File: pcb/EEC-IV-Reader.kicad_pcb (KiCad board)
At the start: 2 copper layers, 53 x 68.7 mm, 39 parts, among them J1 ARDUINO_1, J2 ARDUINO_2, J3 RS_485_DEBUG, J4 ARDUINO_3, J5 ARDUINO_4, J6 DISPLAY, J7 OBD, J8 I2C_DEBUG, J9 Vin_disconnect, SW1 BTN_UP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

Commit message: Update LED Labels and Diode direction
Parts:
- moved D2 7.60 mm to (87.6, 61.3), turned to 180 degrees
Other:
- board text added: "IN"
- board text added: "OUT"
- board text added: "v0.4"
- board text removed: "DI"
- board text removed: "RO"
- board text removed: "v0.3"
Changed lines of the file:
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@@
   )
   (footprint "Diode_THT:D_A-405_P7.62mm_Horizontal" (layer "F.Cu")
-    (at 80 61.3)
+    (at 87.6 61.3 180)
     (descr "Diode, A-405 series, Axial, Horizontal, pin pitch=7.62mm, , length*diameter=5.2*2.7mm^2, , http://www.diodes.com/_files/packages/A-405.pdf")
     (tags "Diode A-405 series Axial Horizontal pin pitch 7.62mm  length 5.2mm diameter 2.7mm")
@@
     (property "Sheetname" "")
     (attr through_hole)
-    (fp_text reference "D2" (at 3.81 -2.47) (layer "F.SilkS")
+    (fp_text reference "D2" (at 3.85 2.3) (layer "F.SilkS")
       (effects (font (size 1 1) (thickness 0.15)))
     )
@@
     (fp_line (start 1.21 -1.35) (end 1.21 1.35) (layer "F.Fab") (width 0.1))
     (fp_line (start 1.89 -1.35) (end 1.89 1.35) (layer "F.Fab") (width 0.1))
-    (pad "1" thru_hole rect (at 0 0) (size 1.8 1.8) (drill 0.9) (layers *.Cu *.Mask)
+    (pad "1" thru_hole rect (at 0 0 180) (size 1.8 1.8) (drill 0.9) (layers *.Cu *.Mask)
       (net 36 "/8V") (pinfunction "K") (pintype "passive"))
-    (pad "2" thru_hole oval (at 7.62 0) (size 1.8 1.8) (drill 0.9) (layers *.Cu *.Mask)
+    (pad "2" thru_hole oval (at 7.62 0 180) (size 1.8 1.8) (drill 0.9) (layers *.Cu *.Mask)
       (net 5 "Net-(D2-Pad2)") (pinfunction "A") (pintype "passive"))
     (model "${KICAD6_3DMODEL_DIR}/Diode_THT.3dshapes/D_A-405_P7.62mm_Horizontal.wrl"
@@
     (effects (font (size 1 1) (thickness 0.1)))
   )
-  (gr_text "DI" (at 56 78.9) (layer "F.SilkS")
-    (effects (font (size 1 1) (thickness 0.1)))
-  )
-  (gr_text "v0.3" (at 43.771725 88.904421) (layer "F.SilkS")
+  (gr_text "OUT" (at 56.3 79.05) (layer "F.SilkS")
+    (effects (font (size 1 1) (thickness 0.1)))
+  )
+  (gr_text "v0.4" (at 43.771725 88.904421) (layer "F.SilkS")
     (effects (font (size 1 1) (thickness 0.15)) (justify left))
   )
@@
     (effects (font (size 1 1) (thickness 0.1)))
   )
-  (gr_text "RO" (at 56.2 73.5) (layer "F.SilkS")
-    (effects (font (size 1 1) (thickness 0.1)))
-  )
+  (gr_text "IN" (at 55.8 73.45) (layer "F.SilkS")
+    (effects (font (size 1 1) (thickness 0.1)))
+  )

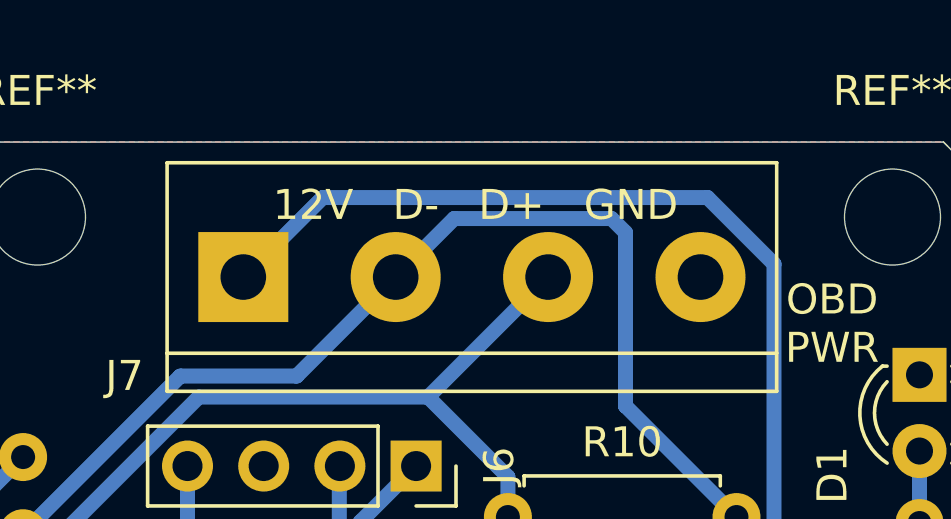
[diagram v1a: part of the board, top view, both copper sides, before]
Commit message: Add terminal labels to backside
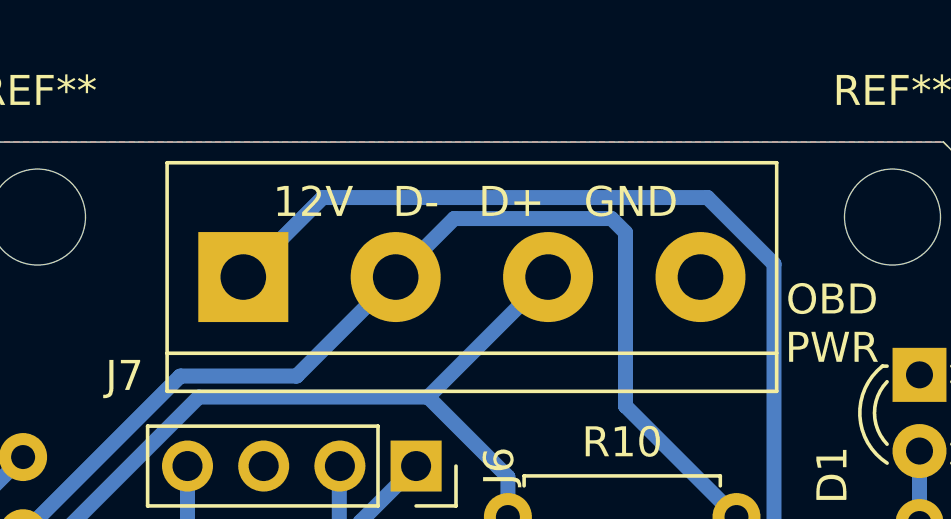
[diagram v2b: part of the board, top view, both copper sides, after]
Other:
- board text added: "GND D+ D- 12V"
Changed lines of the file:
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@@
   (gr_line (start 40 95.7) (end 93 95.7) (layer "Edge.Cuts") (width 0.05))
   (gr_line (start 87.7 27) (end 55.1 27) (layer "Edge.Cuts") (width 0.05))
+  (gr_text "GND   D+   D-   12V" (at 71.8 29) (layer "B.SilkS")
+    (effects (font (size 1 1) (thickness 0.1)) (justify mirror))
+  )
   (gr_text "GND" (at 46.3 47.5) (layer "F.SilkS")
     (effects (font (size 1 1) (thickness 0.1)))
@@
     (effects (font (size 1.5 1.5) (thickness 0.3)) (justify left))
   )
-  (gr_text "12V   D-   D+   GND" (at 72.1 29.1) (layer "F.SilkS")
+  (gr_text "12V   D-   D+   GND" (at 72.1 29) (layer "F.SilkS")
     (effects (font (size 1 1) (thickness 0.1)))
   )
